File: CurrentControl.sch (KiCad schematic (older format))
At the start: 10 parts, among them P1 HEATSINK, Q401 BUK9575, U201 LMV358

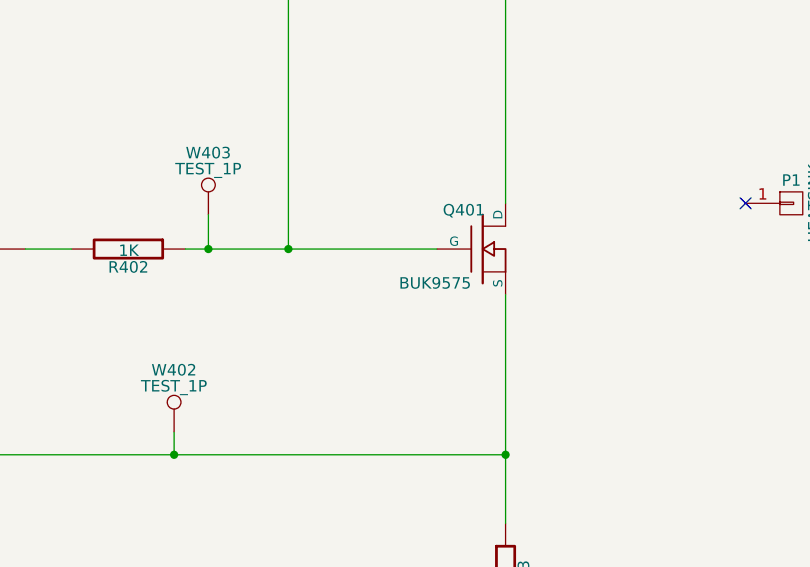
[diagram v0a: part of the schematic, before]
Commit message: revised resistors to match available values, replaced FET (old FET was obsolete/unavail)
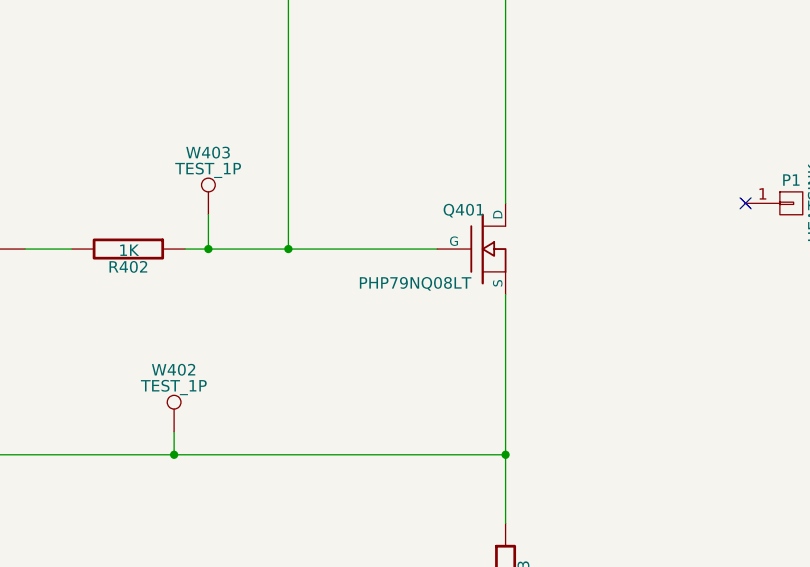
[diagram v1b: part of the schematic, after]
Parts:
- Q401: value BUK9575 -> PHP79NQ08LT; Fieldname (none) -> Old Value -> BUK9575-100A,127; MPN BUK9575-100A,127 -> PHP79NQ08LT,127
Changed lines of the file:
@@
 P 8000 3700
 F 0 "Q401" H 8010 3870 50  0000 R CNN
-F 1 "BUK9575" H 7950 3550 50  0000 R CNN
+F 1 "PHP79NQ08LT" H 7950 3550 50  0000 R CNN
 F 2 "Current:TO-220_FET-GDS_Vertical" H 8000 3700 60  0001 C CNN
-F 3 "" H 8000 3700 60  0000 C CNN
-F 4 "BUK9575-100A,127" H 8000 3700 60  0001 C CNN "MPN"
+F 3 "http://www.nxp.com/documents/data_sheet/PHP79NQ08LT.pdf" H 8000 3700 60  0001 C CNN
+F 4 "Old Value -> BUK9575-100A,127" H 8000 3700 60  0001 C CNN "Fieldname"
+F 5 "PHP79NQ08LT,127" H 8000 3700 60  0001 C CNN "MPN"
 	1    8000 3700
 	1    0    0    -1
 $EndComp
 $Comp
-L GND #PWR401
+L GND #PWR06
 U 1 1 54DADC82
 P 5400 4250
-F 0 "#PWR401" H 5400 4000 60  0001 C CNN
+F 0 "#PWR06" H 5400 4000 60  0001 C CNN
 F 1 "GND" H 5400 4100 60  0000 C CNN
 F 2 "" H 5400 4250 60  0000 C CNN

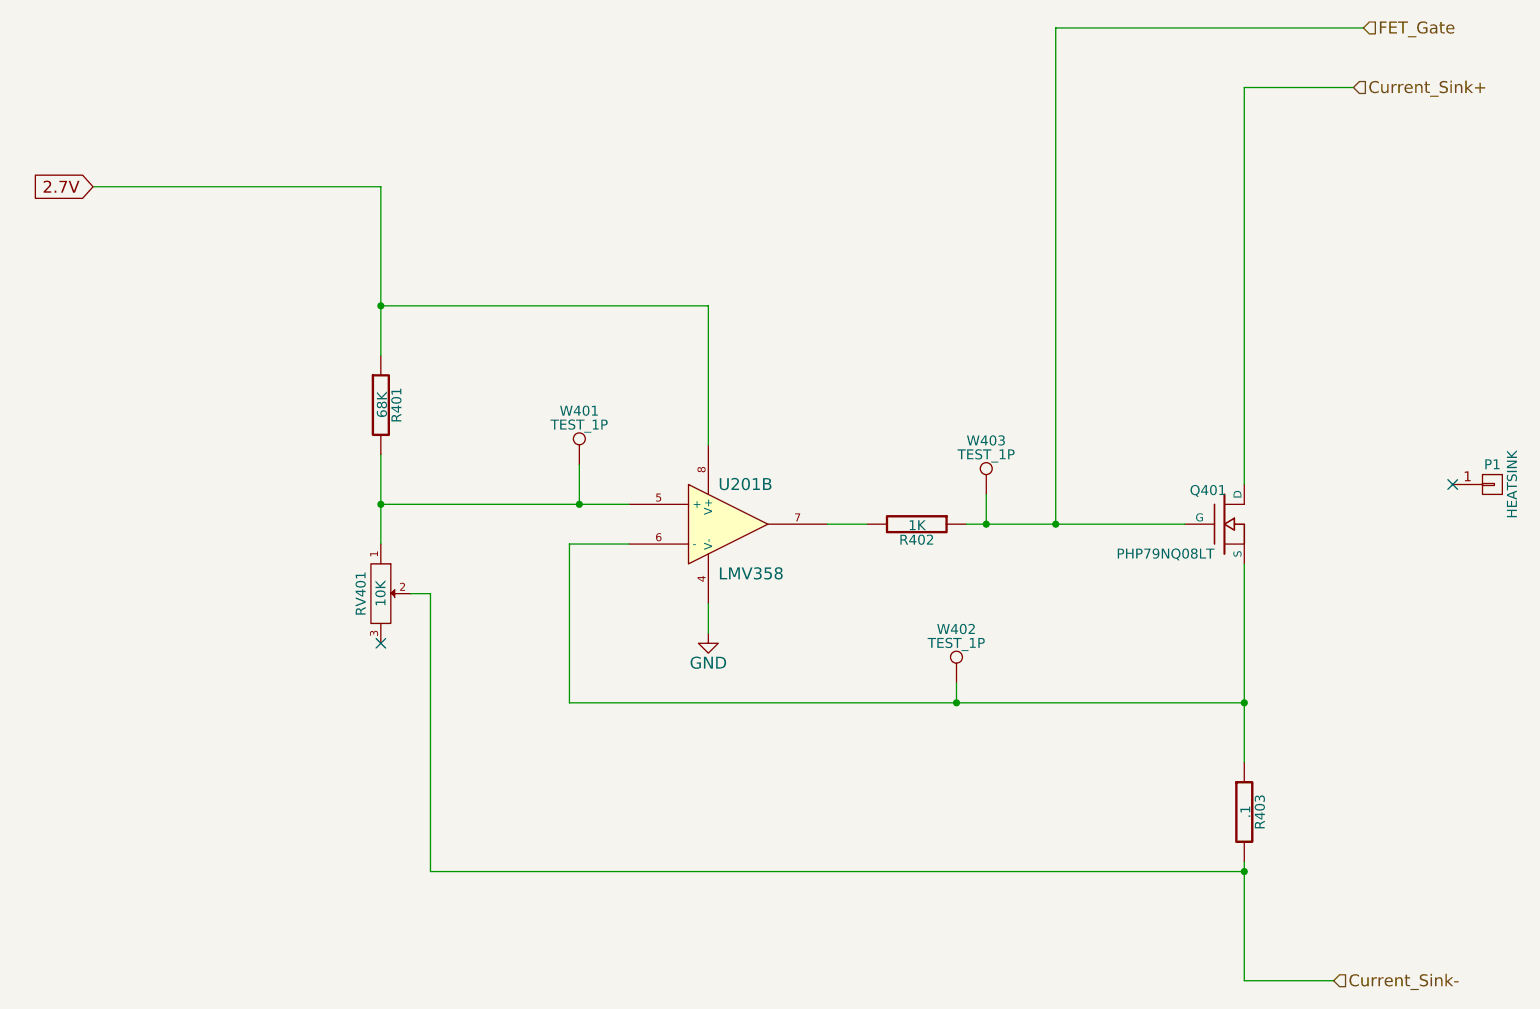
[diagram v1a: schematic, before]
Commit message: added fine-gain pot to the current control sheet
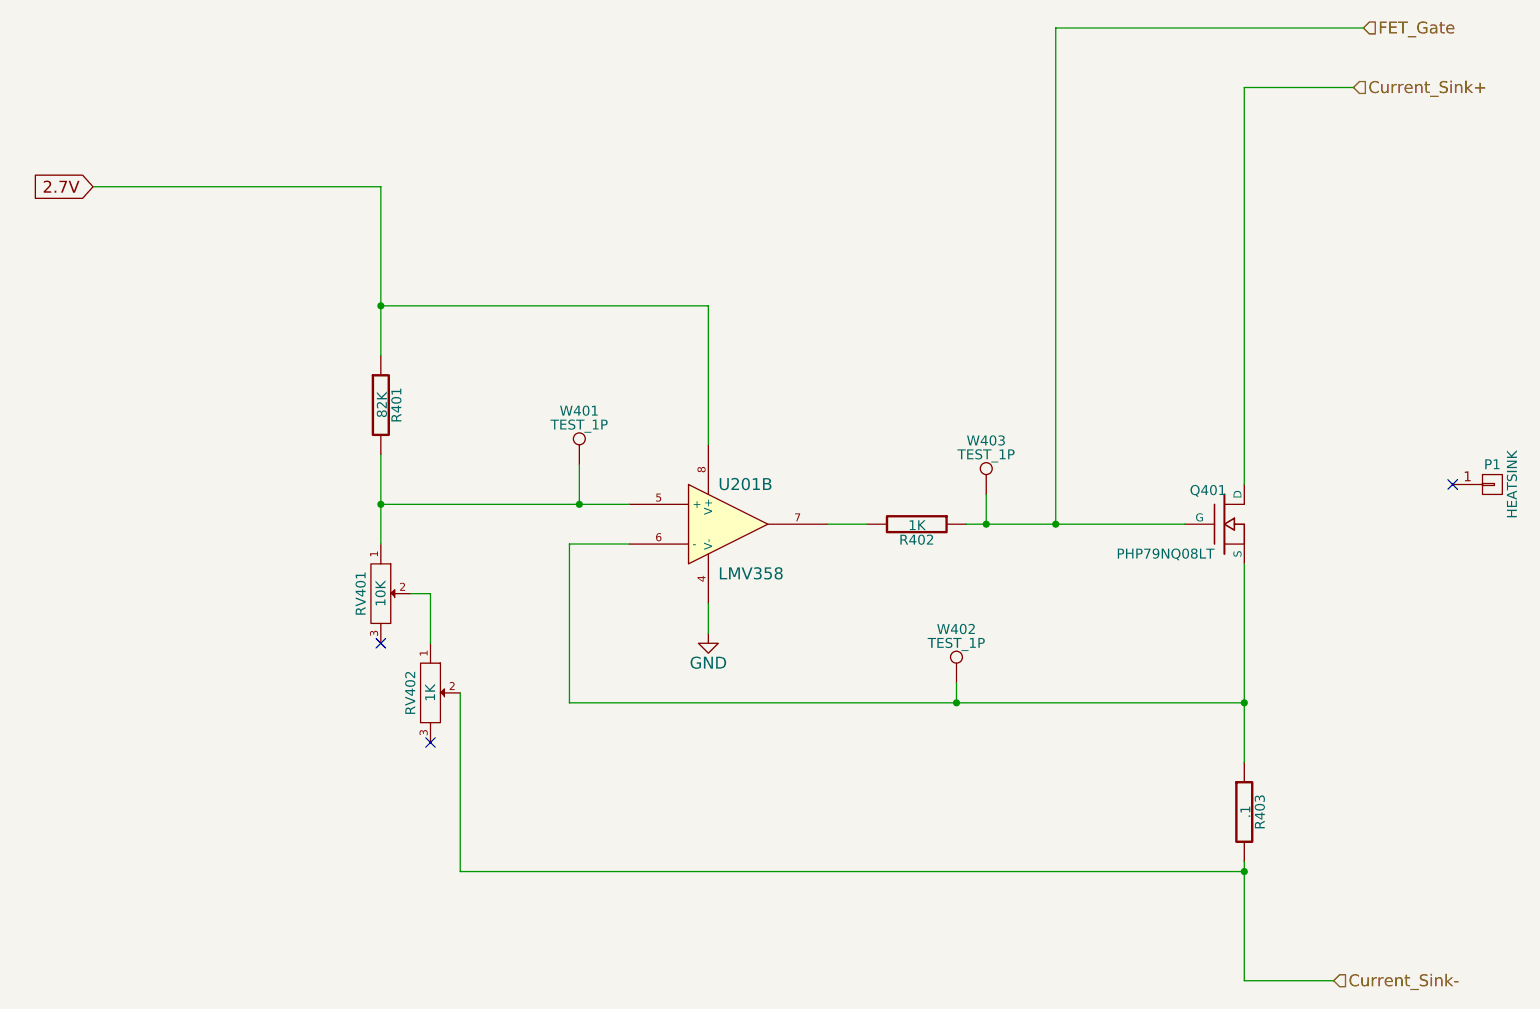
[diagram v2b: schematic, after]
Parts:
- added RV402: 1K, symbol POT-RESCUE-CurrentSinkOrSwim
- R401: value 68K -> 82K
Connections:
- net Current_Sink-: now also RV402.2; no longer RV401.2
- new net: RV401.2, RV402.1
- no-connect marks 2 -> 3
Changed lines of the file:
@@
 $EndComp
 $Comp
-L GND #PWR06
+L GND #PWR401
 U 1 1 54DADC82
 P 5400 4250
-F 0 "#PWR06" H 5400 4000 60  0001 C CNN
+F 0 "#PWR401" H 5400 4000 60  0001 C CNN
 F 1 "GND" H 5400 4100 60  0000 C CNN
 F 2 "" H 5400 4250 60  0000 C CNN
@@
 P 3750 3100
 F 0 "R401" V 3830 3100 50  0000 C CNN
-F 1 "68K" V 3757 3101 50  0000 C CNN
+F 1 "82K" V 3757 3101 50  0000 C CNN
 F 2 "Resistors_SMD:R_0805" V 3680 3100 30  0001 C CNN
 F 3 "" H 3750 3100 30  0000 C CNN
@@
 	3900 4050 4000 4050
 Wire Wire Line
-	4000 4050 4000 5450
-Wire Wire Line
-	4000 5450 8100 5450
+	4150 5450 8100 5450
 NoConn ~ 3750 4300
 NoConn ~ 9150 3500
@@
 	6800 3550 6800 3700
 Connection ~ 6800 3700
+$Comp
+L POT-RESCUE-CurrentSinkOrSwim RV402
+U 1 1 57EAA830
+P 4000 4550
+F 0 "RV402" H 4000 4450 50  0000 C CNN
+F 1 "1K" H 4000 4550 50  0000 C CNN
+F 2 "" H 4000 4550 60  0001 C CNN
+F 3 "" H 4000 4550 60  0000 C CNN
+F 4 "Value" H 4000 4550 60  0001 C CNN "Fieldname"
+F 5 "P110KV1-1F25BR1K" H 4000 4550 60  0001 C CNN "MPN"
+	1    4000 4550
+	0    1    1    0
+$EndComp
+Wire Wire Line
+	4000 4050 4000 4300
+Wire Wire Line
+	4150 4550 4150 5450
+NoConn ~ 4000 4800
 $EndSCHEMATC

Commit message: Revert "added fine-gain pot to the current control sheet"
This reverts commit 2c8c25b55c9f8694f13c8f60d96001b4a7e97e34.
After testing the Rev. 1, didn't need the fine gain potentiometer
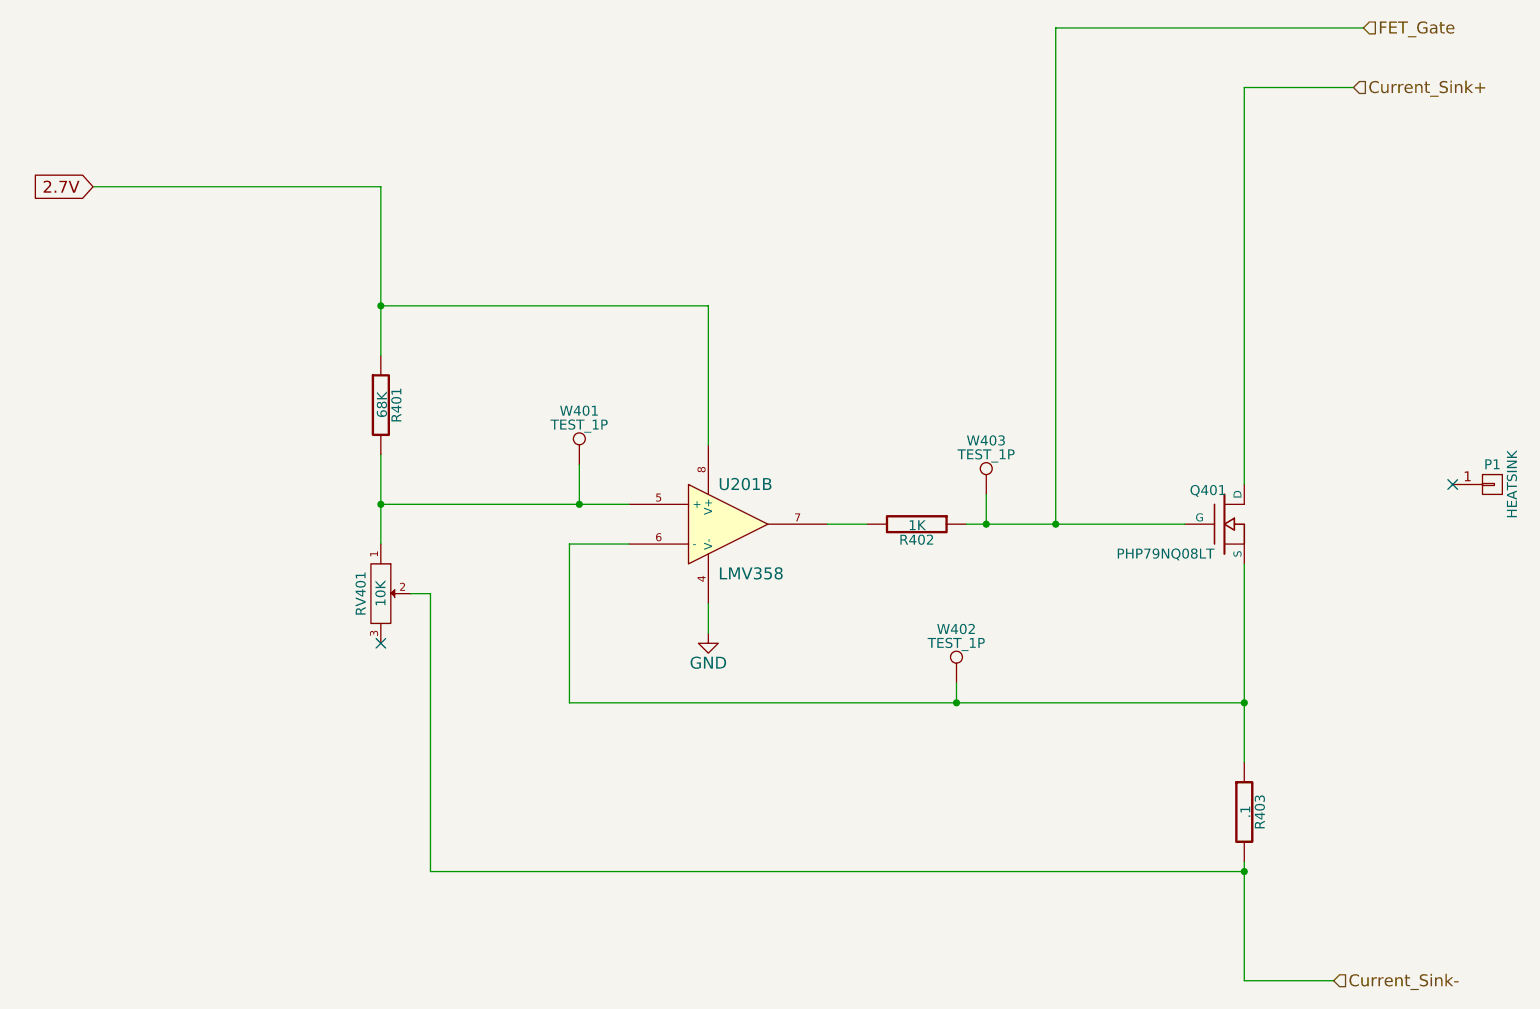
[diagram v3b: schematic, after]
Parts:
- removed RV402: 1K, symbol POT-RESCUE-CurrentSinkOrSwim
- R401: value 82K -> 68K
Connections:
- net Current_Sink-: now also RV401.2
- no-connect marks 3 -> 2
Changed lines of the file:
@@
 $EndComp
 $Comp
-L GND #PWR401
+L GND #PWR06
 U 1 1 54DADC82
 P 5400 4250
-F 0 "#PWR401" H 5400 4000 60  0001 C CNN
+F 0 "#PWR06" H 5400 4000 60  0001 C CNN
 F 1 "GND" H 5400 4100 60  0000 C CNN
 F 2 "" H 5400 4250 60  0000 C CNN
@@
 P 3750 3100
 F 0 "R401" V 3830 3100 50  0000 C CNN
-F 1 "82K" V 3757 3101 50  0000 C CNN
+F 1 "68K" V 3757 3101 50  0000 C CNN
 F 2 "Resistors_SMD:R_0805" V 3680 3100 30  0001 C CNN
 F 3 "" H 3750 3100 30  0000 C CNN
@@
 	3900 4050 4000 4050
 Wire Wire Line
-	4150 5450 8100 5450
+	4000 4050 4000 5450
+Wire Wire Line
+	4000 5450 8100 5450
 NoConn ~ 3750 4300
 NoConn ~ 9150 3500
@@
 	6800 3550 6800 3700
 Connection ~ 6800 3700
-$Comp
-L POT-RESCUE-CurrentSinkOrSwim RV402
-U 1 1 57EAA830
-P 4000 4550
-F 0 "RV402" H 4000 4450 50  0000 C CNN
-F 1 "1K" H 4000 4550 50  0000 C CNN
-F 2 "" H 4000 4550 60  0001 C CNN
-F 3 "" H 4000 4550 60  0000 C CNN
-F 4 "Value" H 4000 4550 60  0001 C CNN "Fieldname"
-F 5 "P110KV1-1F25BR1K" H 4000 4550 60  0001 C CNN "MPN"
-	1    4000 4550
-	0    1    1    0
-$EndComp
-Wire Wire Line
-	4000 4050 4000 4300
-Wire Wire Line
-	4150 4550 4150 5450
-NoConn ~ 4000 4800
 $EndSCHEMATC
